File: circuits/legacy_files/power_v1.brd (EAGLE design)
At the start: 58.1 x 34 mm, 22 parts

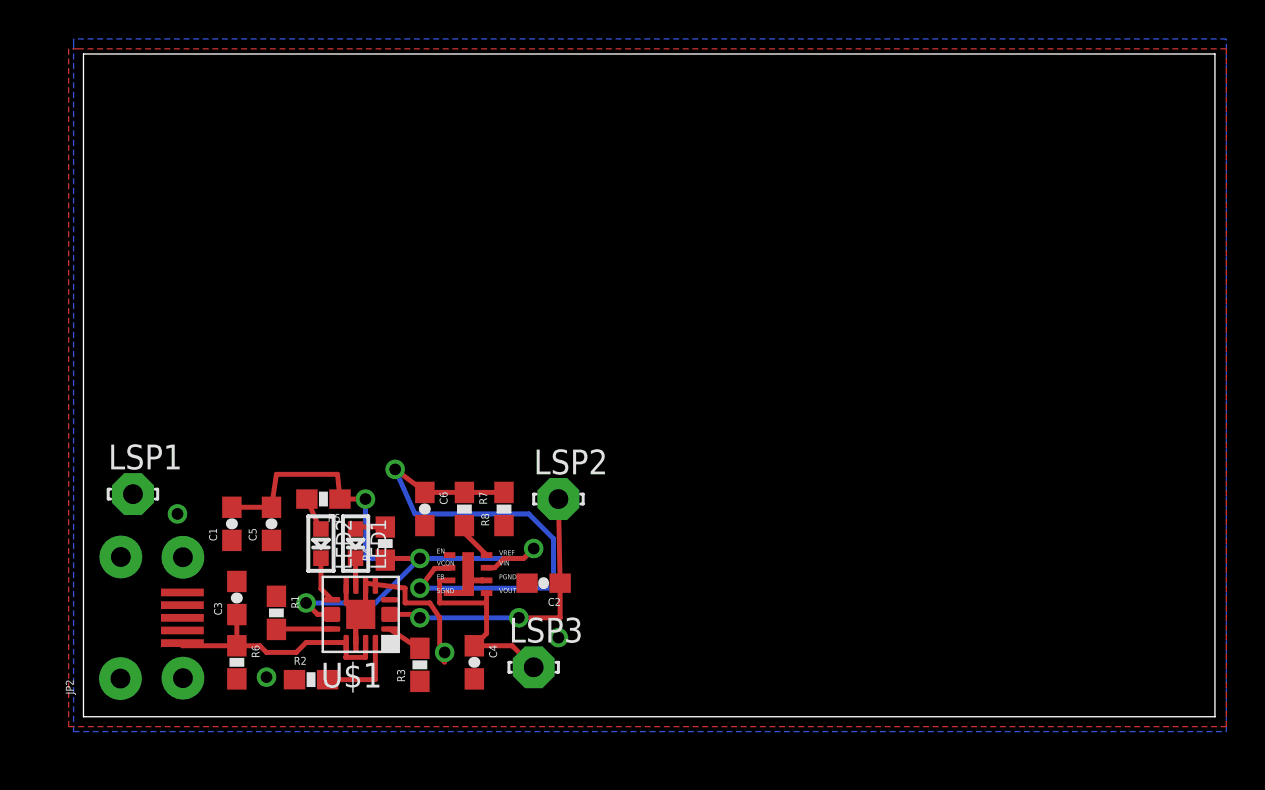
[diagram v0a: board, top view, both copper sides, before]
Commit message: changed LMZ10500 library. updated power schematic and switched out usb. Made new power layout.
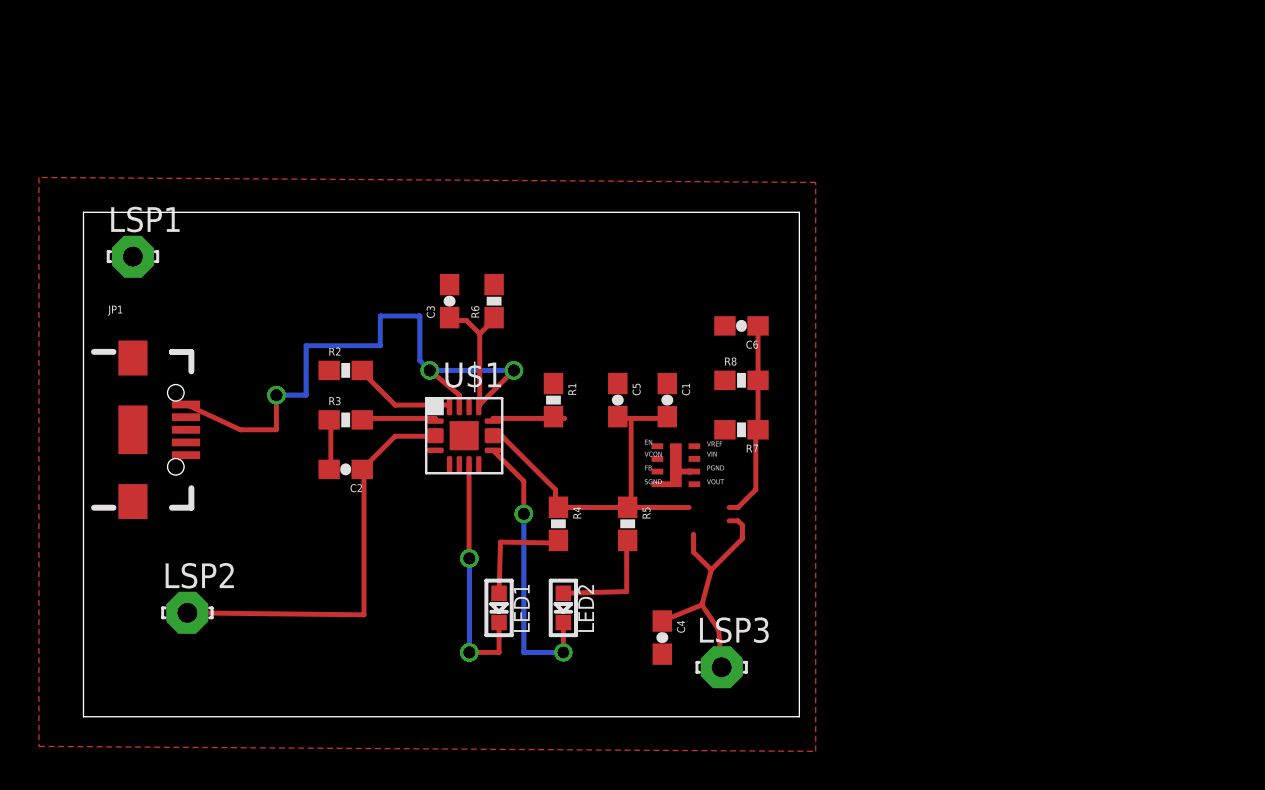
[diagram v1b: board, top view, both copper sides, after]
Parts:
- removed JP2: (no value), SparkFun-Connectors:MICRO-B-SMT
- added JP1: (no value), SparkFun-Connectors:USB-B-MICRO-SMD_V03
- moved C1 23.2 mm to (30.0, 16.3), turned to 270 degrees
- moved R6 22.8 mm to (21.1, 21.3), turned to 90 degrees
- moved LSP2 19.9 mm to (5.33, 5.33)
- moved C5 18.9 mm to (27.4, 16.3), turned to 270 degrees
- moved C6 18.8 mm to (33.8, 20.1), turned to 180 degrees
- moved C3 18.7 mm to (18.8, 21.3)
- moved R1 17.9 mm to (24.1, 16.3)
- moved R2 16.0 mm to (13.5, 17.8)
- moved R5 15.7 mm to (27.9, 9.91), turned to 270 degrees
- moved R7 14.8 mm to (33.8, 14.7), turned to 180 degrees
- moved R8 13.9 mm to (33.8, 17.3), turned to 0 degrees
- moved R3 13.1 mm to (13.5, 15.2), turned to 0 degrees
- moved LED2 12.9 mm to (24.6, 5.59)
- moved LSP1 12.2 mm to (2.54, 23.6)
- moved U$2 12.0 mm to (29.5, 11.9)
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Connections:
- new net N$8: C1.1, C2.2, C3.2, C4.2, C5.1, C6.2, JP1.GND1, LSP1.MP, R1.1, R2.1, R3.1, R6.2, R8.1, U$1.14, U$1.4, U$1.5, U$1.6, U$1.8
- net GND: no longer C1.1, C2.2, C3.2, C4.2, C5.1, C6.2, JP2.5, LSP1.MP, R1.1, R2.1, R3.1, R6.2, R8.1, U$1.14, U$1.4, U$1.5, U$1.6, U$1.8
- net N$14: now also JP1.VBUS1; no longer JP2.1
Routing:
- net N$14: track 13.0 -> 37.4 mm, vias 0 -> 3
- net GND: track 18.2 -> 0.00 mm, vias 4 -> 0
- net N$2: track 27.6 -> 10.4 mm, vias 2 -> 0
- net N$9: track 34.4 -> 19.3 mm, vias 4 -> 0
- net N$12: track 2.37 -> 14.6 mm, vias 0 -> 2
- net N$13: track 1.42 -> 12.7 mm, vias 0 -> 2
- net BAT: track 14.9 -> 21.1 mm, vias 2 -> 0
- net N$10: track 1.62 -> 5.84 mm
- net N$11: track 1.71 -> 5.89 mm
- net VOUT: track 10.5 -> 13.5 mm
- net N$19: track 0.00 -> 2.54 mm
- net N$6: track 1.88 -> 3.91 mm
- net N$1: track 1.99 -> 0.00 mm
- net N$3: track 2.86 -> 4.36 mm
- net N$5: track 4.33 -> 5.32 mm
- added copper zone on layer 1, net N$8
- removed copper zone on layer 1, net GND
- removed copper zone on layer 16, net GND
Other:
- board size 58.1 x 34 mm -> 36.8 x 25.9 mm
